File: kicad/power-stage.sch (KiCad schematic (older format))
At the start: 11 parts, among them Q1 KND3508A, U7 PN7006A

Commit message: WIP Layout, TODO: DRC
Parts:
- D7: footprint Diode_SMD:D_SMA -> htl_smd:D_SMA_wide
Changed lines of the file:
@@
 F 0 "D7" H 4000 2275 50  0000 C CNN
 F 1 "SS210" H 4000 2366 50  0000 C CNN
-F 2 "Diode_SMD:D_SMA" H 4000 2500 50  0001 C CNN
+F 2 "htl_smd:D_SMA_wide" H 4000 2500 50  0001 C CNN
 F 3 "~" H 4000 2500 50  0001 C CNN
 F 4 "C2683692" H 4000 2500 50  0001 C CNN "DistOrderNr"

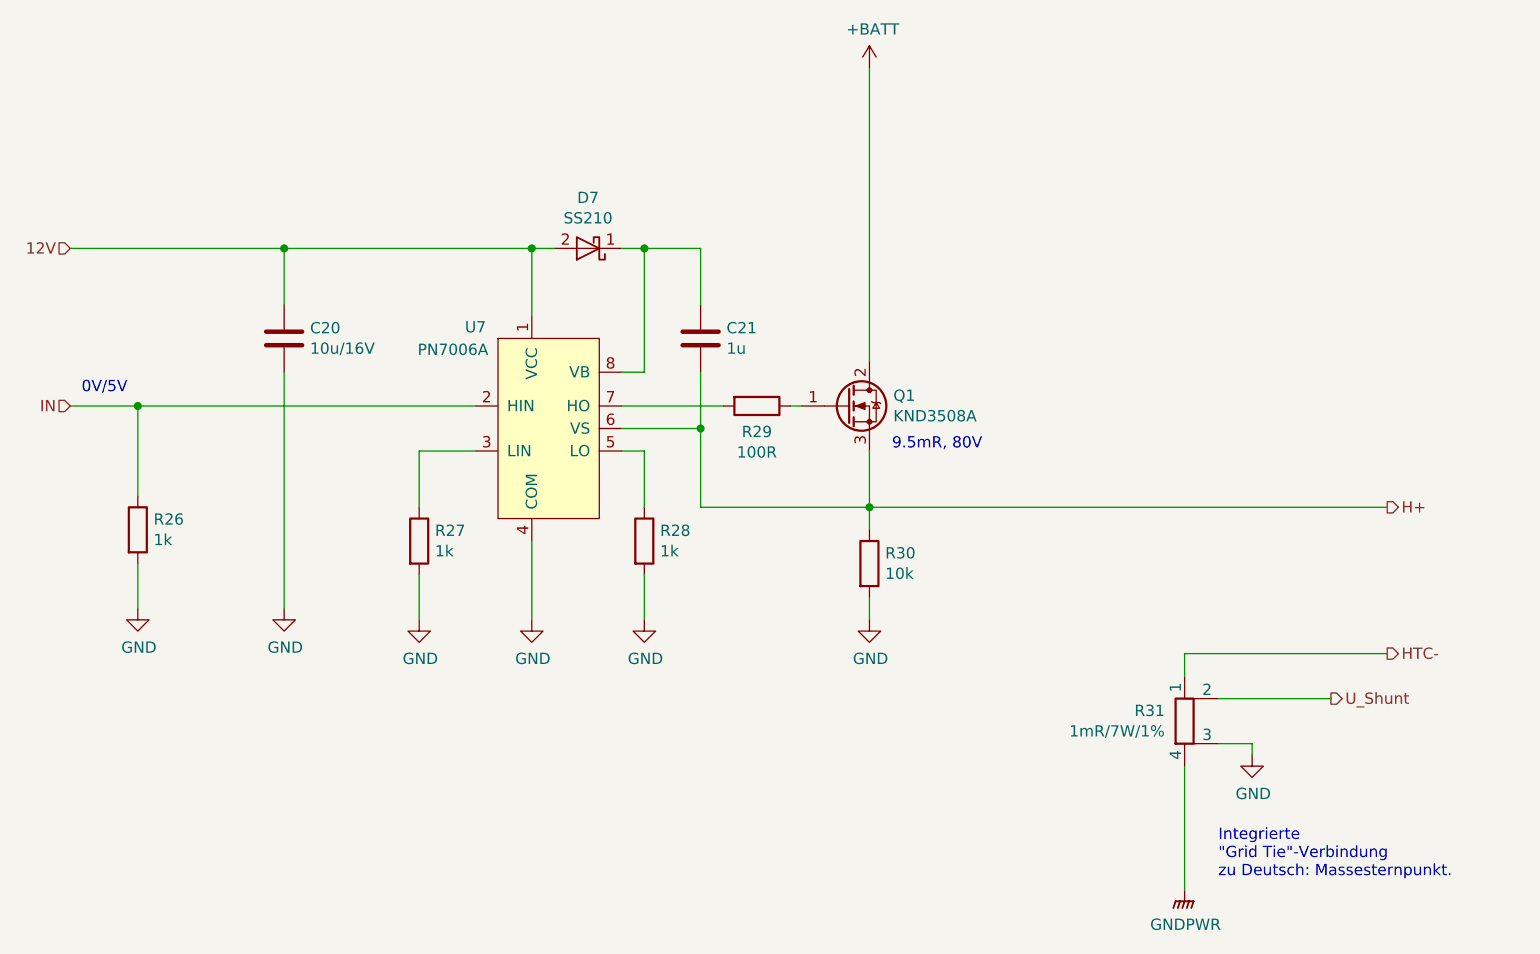
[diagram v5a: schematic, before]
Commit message: Hardware-Anpassungen bei Inbetriebnahme und Firmwareaktualisierung
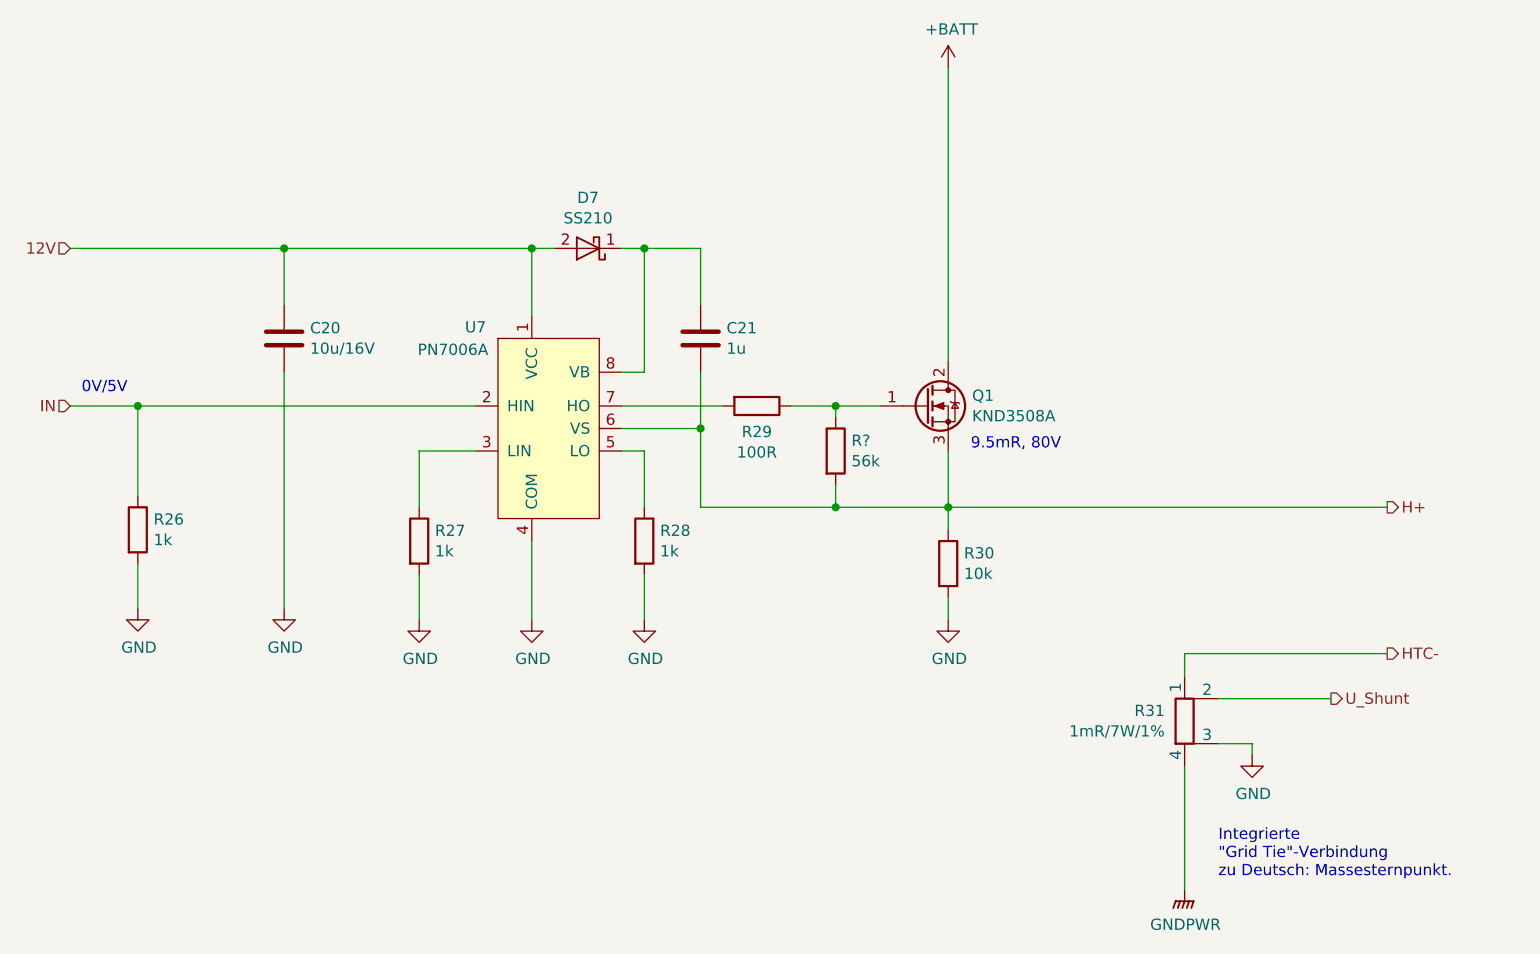
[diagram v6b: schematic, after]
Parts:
- added R?: 56k, Resistor_SMD:R_1206_3216Metric, symbol Device:R
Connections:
- net H+: now also R?.2
- net at Q1.1 (G), R29.1: now also R?.1
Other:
- moved on the sheet: Q1, R30
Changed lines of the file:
@@
 L Device:Q_NMOS_GDS Q1
 U 1 1 609F807E
-P 5150 3200
-F 0 "Q1" H 5356 3246 50  0000 L CNN
-F 1 "KND3508A" H 5356 3155 50  0000 L CNN
-F 2 "Package_TO_SOT_SMD:TO-252-2" H 5350 3300 50  0001 C CNN
-F 3 "~" H 5150 3200 50  0001 C CNN
-F 4 "KIA Semicon Tech" H 5150 3200 50  0001 C CNN "Manufacturer"
-F 5 "KND3508A" H 5150 3200 50  0001 C CNN "ManPartNr"
-F 6 "LCSC" H 5150 3200 50  0001 C CNN "Distributor"
-F 7 "C116513" H 5150 3200 50  0001 C CNN "DistOrderNr"
-F 8 "0.226" H 5150 3200 50  0001 C CNN "PriceEUR"
-F 9 "100" H 5150 3200 50  0001 C CNN "PriceForQty"
-F 10 "https://lcsc.com/product-detail/MOSFET_KIA-Semicon-Tech-KND3508A_C116513.html" H 5150 3200 50  0001 C CNN "Weblink"
-	1    5150 3200
+P 5500 3200
+F 0 "Q1" H 5706 3246 50  0000 L CNN
+F 1 "KND3508A" H 5706 3155 50  0000 L CNN
+F 2 "Package_TO_SOT_SMD:TO-252-2" H 5700 3300 50  0001 C CNN
+F 3 "~" H 5500 3200 50  0001 C CNN
+F 4 "KIA Semicon Tech" H 5500 3200 50  0001 C CNN "Manufacturer"
+F 5 "KND3508A" H 5500 3200 50  0001 C CNN "ManPartNr"
+F 6 "LCSC" H 5500 3200 50  0001 C CNN "Distributor"
+F 7 "C116513" H 5500 3200 50  0001 C CNN "DistOrderNr"
+F 8 "0.226" H 5500 3200 50  0001 C CNN "PriceEUR"
+F 9 "100" H 5500 3200 50  0001 C CNN "PriceForQty"
+F 10 "https://lcsc.com/product-detail/MOSFET_KIA-Semicon-Tech-KND3508A_C116513.html" H 5500 3200 50  0001 C CNN "Weblink"
+	1    5500 3200
 	1    0    0    -1
 $EndComp
@@
 L Device:R R30
 U 1 1 609FB915
-P 5250 3900
-F 0 "R30" H 5320 3946 50  0000 L CNN
-F 1 "10k" H 5320 3855 50  0000 L CNN
-F 2 "Resistor_SMD:R_1206_3216Metric" V 5180 3900 50  0001 C CNN
-F 3 "~" H 5250 3900 50  0001 C CNN
-F 4 "0.01" H 5250 3900 50  0001 C CNN "PriceEUR"
-F 5 "C118075" H 5250 3900 50  0001 C CNN "DistOrderNr"
-F 6 "LCSC" H 5250 3900 50  0001 C CNN "Distributor"
-	1    5250 3900
+P 5600 3900
+F 0 "R30" H 5670 3946 50  0000 L CNN
+F 1 "10k" H 5670 3855 50  0000 L CNN
+F 2 "Resistor_SMD:R_1206_3216Metric" V 5530 3900 50  0001 C CNN
+F 3 "~" H 5600 3900 50  0001 C CNN
+F 4 "0.01" H 5600 3900 50  0001 C CNN "PriceEUR"
+F 5 "C118075" H 5600 3900 50  0001 C CNN "DistOrderNr"
+F 6 "LCSC" H 5600 3900 50  0001 C CNN "Distributor"
+	1    5600 3900
 	1    0    0    -1
 $EndComp
@@
 	4500 3300 4500 3650
 Wire Wire Line
-	4500 3650 5250 3650
-Wire Wire Line
-	5250 3400 5250 3650
-Connection ~ 5250 3650
-Wire Wire Line
-	5250 3650 5250 3750
+	4500 3650 5100 3650
+Wire Wire Line
+	5600 3400 5600 3650
+Connection ~ 5600 3650
+Wire Wire Line
+	5600 3650 5600 3750
 $Comp
 L Device:C C21
@@
 L power:+BATT #PWR042
 U 1 1 60A0291F
-P 5250 1700
-F 0 "#PWR042" H 5250 1550 50  0001 C CNN
-F 1 "+BATT" H 5265 1873 50  0000 C CNN
-F 2 "" H 5250 1700 50  0001 C CNN
-F 3 "" H 5250 1700 50  0001 C CNN
-	1    5250 1700
-	1    0    0    -1
-$EndComp
-Wire Wire Line
-	5250 1700 5250 3000
+P 5600 1700
+F 0 "#PWR042" H 5600 1550 50  0001 C CNN
+F 1 "+BATT" H 5615 1873 50  0000 C CNN
+F 2 "" H 5600 1700 50  0001 C CNN
+F 3 "" H 5600 1700 50  0001 C CNN
+	1    5600 1700
+	1    0    0    -1
+$EndComp
+Wire Wire Line
+	5600 1700 5600 3000
 Text HLabel 1700 2500 0    50   Input ~ 0
 12V
@@
 L power:GND #PWR043
 U 1 1 60A05E12
-P 5250 4150
-F 0 "#PWR043" H 5250 3900 50  0001 C CNN
-F 1 "GND" H 5255 3977 50  0000 C CNN
-F 2 "" H 5250 4150 50  0001 C CNN
-F 3 "" H 5250 4150 50  0001 C CNN
-	1    5250 4150
-	1    0    0    -1
-$EndComp
-Wire Wire Line
-	5250 4150 5250 4050
+P 5600 4150
+F 0 "#PWR043" H 5600 3900 50  0001 C CNN
+F 1 "GND" H 5605 3977 50  0000 C CNN
+F 2 "" H 5600 4150 50  0001 C CNN
+F 3 "" H 5600 4150 50  0001 C CNN
+	1    5600 4150
+	1    0    0    -1
+$EndComp
+Wire Wire Line
+	5600 4150 5600 4050
 $Comp
 L power:GND #PWR040
@@
 	6650 4300 7550 4300
 Wire Wire Line
-	5250 3650 7550 3650
+	5600 3650 7550 3650
 $Comp
 L power:GNDPWR #PWR044
@@
 Text HLabel 7550 3650 2    50   Output ~ 0
 H+
-Text Notes 5350 3400 0    50   ~ 0
+Text Notes 5700 3400 0    50   ~ 0
 9.5mR, 80V
 Wire Wire Line
@@
 $EndComp
 Wire Wire Line
-	4900 3200 4950 3200
+	4900 3200 5100 3200
 Wire Wire Line
 	6650 4800 6650 5350
 Text Notes 6800 5300 0    50   ~ 0
 Integrierte\n"Grid Tie"-Verbindung\nzu Deutsch: Massesternpunkt.
+$Comp
+L Device:R R?
+U 1 1 60CD69B2
+P 5100 3400
+F 0 "R?" H 5170 3446 50  0000 L CNN
+F 1 "56k" H 5170 3355 50  0000 L CNN
+F 2 "Resistor_SMD:R_1206_3216Metric" V 5030 3400 50  0001 C CNN
+F 3 "~" H 5100 3400 50  0001 C CNN
+F 4 "0.01" H 5100 3400 50  0001 C CNN "PriceEUR"
+F 5 "LCSC" H 5100 3400 50  0001 C CNN "Distributor"
+	1    5100 3400
+	1    0    0    -1
+$EndComp
+Wire Wire Line
+	5100 3200 5100 3250
+Connection ~ 5100 3200
+Wire Wire Line
+	5100 3200 5300 3200
+Wire Wire Line
+	5100 3550 5100 3650
+Connection ~ 5100 3650
+Wire Wire Line
+	5100 3650 5600 3650
 $EndSCHEMATC

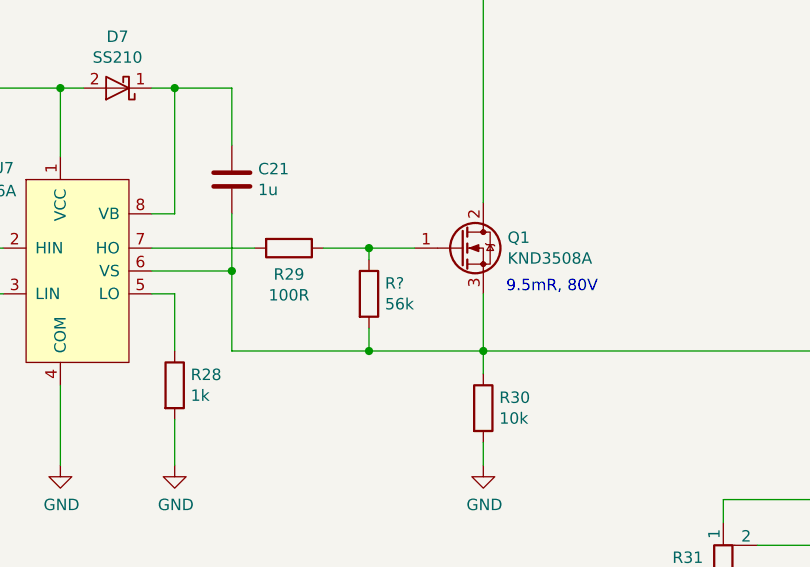
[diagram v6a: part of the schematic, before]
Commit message: HTML-BOM aktualisiert
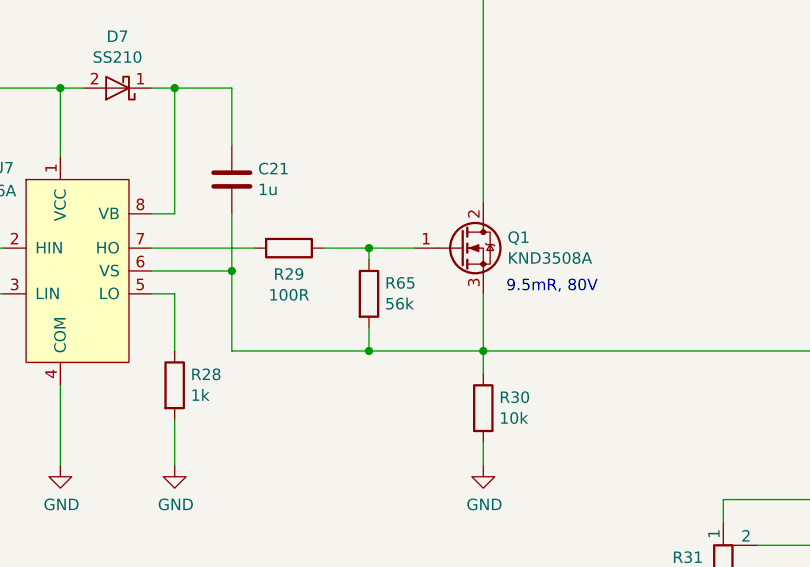
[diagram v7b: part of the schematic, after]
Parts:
- gave numbers to parts that had none: 1
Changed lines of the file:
@@
 Integrierte\n"Grid Tie"-Verbindung\nzu Deutsch: Massesternpunkt.
 $Comp
-L Device:R R?
+L Device:R R65
 U 1 1 60CD69B2
 P 5100 3400
-F 0 "R?" H 5170 3446 50  0000 L CNN
+F 0 "R65" H 5170 3446 50  0000 L CNN
 F 1 "56k" H 5170 3355 50  0000 L CNN
 F 2 "Resistor_SMD:R_1206_3216Metric" V 5030 3400 50  0001 C CNN

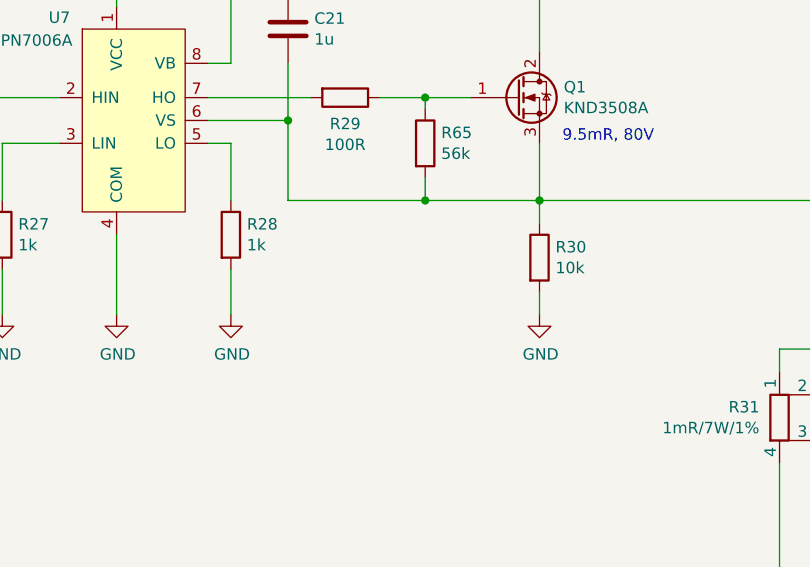
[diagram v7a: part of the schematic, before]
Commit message: Bugfix: Schottky-Diode im Schaltplan
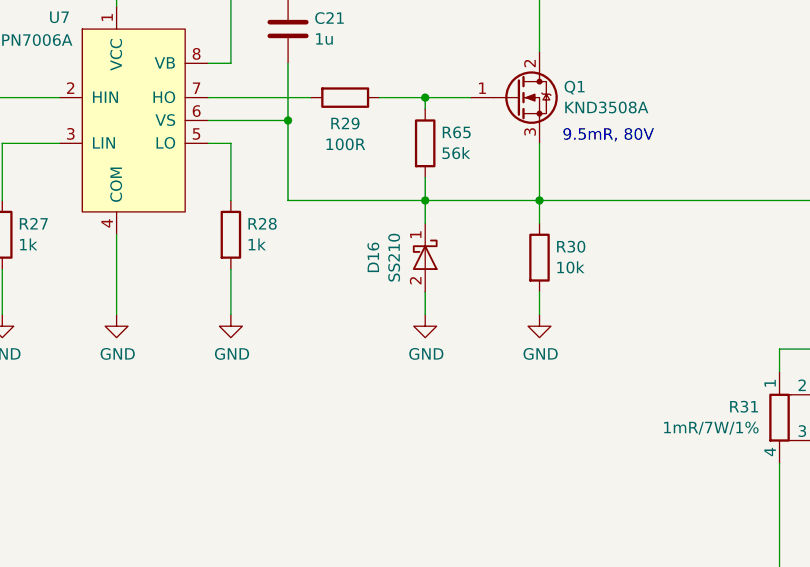
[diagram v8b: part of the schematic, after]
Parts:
- added D16: SS210, htl_smd:D_SMA_wide, symbol htl_semiconductors:D_Schottky
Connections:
- net GND: now also D16.2 (A)
- net H+: now also D16.1 (K)
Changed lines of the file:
@@
 Wire Wire Line
 	5100 3650 5600 3650
+$Comp
+L htl_semiconductors:D_Schottky D16
+U 1 1 60D9E4E3
+P 5100 3900
+F 0 "D16" H 5100 3675 50  0000 C CNN
+F 1 "SS210" H 5100 3766 50  0000 C CNN
+F 2 "htl_smd:D_SMA_wide" H 5100 3900 50  0001 C CNN
+F 3 "~" H 5100 3900 50  0001 C CNN
+F 4 "C2683692" H 5100 3900 50  0001 C CNN "DistOrderNr"
+F 5 "LCSC" H 5100 3900 50  0001 C CNN "Distributor"
+F 6 "SS210A-W" H 5100 3900 50  0001 C CNN "ManPartNr"
+F 7 "ZHIDE" H 5100 3900 50  0001 C CNN "Manufacturer"
+F 8 "100V 2A 850mV @ 2A SMA(DO-214AC) Schottky Barrier Diodes" H 5100 3900 50  0001 C CNN "Notes"
+F 9 "0.0155" H 5100 3900 50  0001 C CNN "PriceEUR"
+F 10 "200" H 5100 3900 50  0001 C CNN "PriceForQty"
+F 11 "https://lcsc.com/product-detail/Schottky-Barrier-Diodes-SBD_ZHIDE-SS210A-W_C2683692.html" H 5100 3900 50  0001 C CNN "Weblink"
+	1    5100 3900
+	0    1    1    0
+$EndComp
+$Comp
+L power:GND #PWR064
+U 1 1 60D9F0D3
+P 5100 4150
+F 0 "#PWR064" H 5100 3900 50  0001 C CNN
+F 1 "GND" H 5105 3977 50  0000 C CNN
+F 2 "" H 5100 4150 50  0001 C CNN
+F 3 "" H 5100 4150 50  0001 C CNN
+	1    5100 4150
+	1    0    0    -1
+$EndComp
+Wire Wire Line
+	5100 4150 5100 4050
+Wire Wire Line
+	5100 3750 5100 3650
 $EndSCHEMATC
